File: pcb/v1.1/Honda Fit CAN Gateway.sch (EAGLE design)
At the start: 23 parts, among them U1 TEENSY_3.1_BASIC, U2 MCP2515TSOP, U3 TJA1050, U4 TJA1050, U5 CB3, X1 CON_10X2F_JAE_MX34020NF1

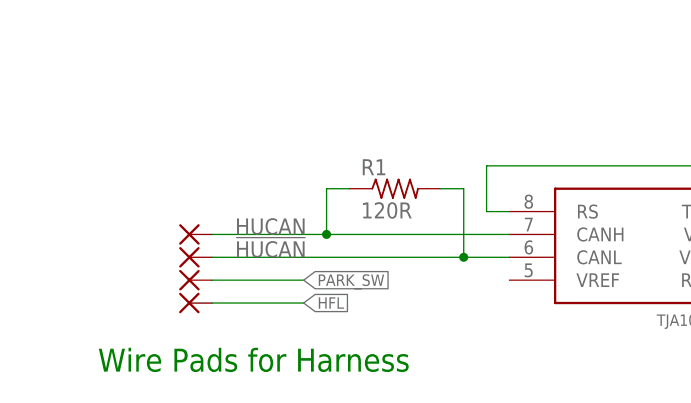
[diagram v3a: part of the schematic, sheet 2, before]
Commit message: Replace discrete pads for output with pin header footprint
Pads were too large on rev 1, and square orientation was not ideal
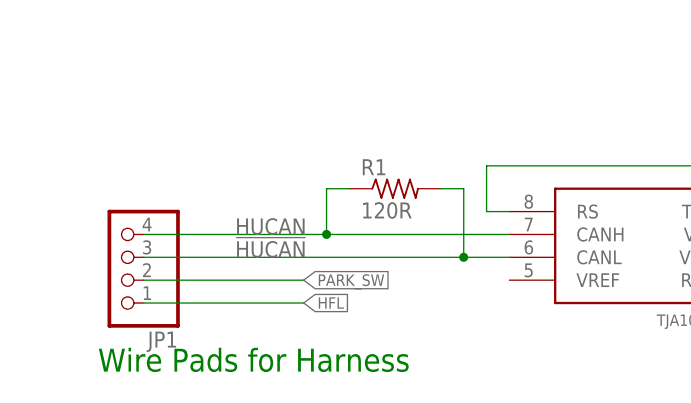
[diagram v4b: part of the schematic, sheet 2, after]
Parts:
- removed PAD1, PAD2, PAD3, PAD4: (no value), wirepad:3,17/1,3
- added JP1: (no value), pinhead:PINHD-1X4
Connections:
- net !HUCAN: now also JP1.3; no longer PAD2.P
- net HFL: now also JP1.1; no longer PAD4.P
- net HUCAN: now also JP1.4; no longer PAD1.P
- net PARK_SW: now also JP1.2; no longer PAD3.P
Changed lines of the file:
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@@
 <part name="SUPPLY2" library="supply2" deviceset="GND" device=""/>
 <part name="P+2" library="supply1" deviceset="+5V" device=""/>
-<part name="PAD1" library="wirepad" deviceset="3,17/1,3" device=""/>
-<part name="PAD2" library="wirepad" deviceset="3,17/1,3" device=""/>
 <part name="FRAME2" library="frames" deviceset="FRAME_A_L" device=""/>
-<part name="PAD3" library="wirepad" deviceset="3,17/1,3" device=""/>
-<part name="PAD4" library="wirepad" deviceset="3,17/1,3" device=""/>
 <part name="FRAME1" library="frames" deviceset="FRAME_A_L" device=""/>
 <part name="P+3" library="supply1" deviceset="+5V" device=""/>
@@
 <part name="C1" library="resistor" deviceset="C-EU" device="C0603" value="100n"/>
 <part name="SUPPLY7" library="supply2" deviceset="GND" device=""/>
+<part name="JP1" library="pinhead" deviceset="PINHD-1X4" device=""/>
 </parts>
 <sheets>
@@
 <attribute name="VALUE" x="208.28" y="147.32" size="1.778" layer="96" rot="R180"/>
 </instance>
-<instance part="PAD1" gate="1" x="88.9" y="71.12" smashed="yes"/>
-<instance part="PAD2" gate="1" x="88.9" y="68.58" smashed="yes"/>
 <instance part="FRAME2" gate="G$1" x="0" y="0"/>
 <instance part="FRAME2" gate="G$2" x="172.72" y="0"/>
-<instance part="PAD3" gate="1" x="88.9" y="66.04" smashed="yes"/>
-<instance part="PAD4" gate="1" x="88.9" y="63.5" smashed="yes"/>
 <instance part="R1" gate="G$1" x="111.76" y="76.2"/>
 <instance part="R4" gate="G$1" x="147.32" y="127"/>
+<instance part="JP1" gate="A" x="81.28" y="68.58" rot="R180"/>
 </instances>
 <busses>
@@
 </segment>
 <segment>
-<pinref part="PAD3" gate="1" pin="P"/>
-<wire x1="91.44" y1="66.04" x2="101.6" y2="66.04" width="0.1524" layer="91"/>
+<wire x1="83.82" y1="66.04" x2="101.6" y2="66.04" width="0.1524" layer="91"/>
 <label x="101.6" y="66.04" size="1.27" layer="95" xref="yes"/>
+<pinref part="JP1" gate="A" pin="2"/>
 </segment>
 </net>
@@
 </segment>
 <segment>
-<pinref part="PAD4" gate="1" pin="P"/>
-<wire x1="91.44" y1="63.5" x2="101.6" y2="63.5" width="0.1524" layer="91"/>
+<wire x1="83.82" y1="63.5" x2="101.6" y2="63.5" width="0.1524" layer="91"/>
 <label x="101.6" y="63.5" size="1.27" layer="95" xref="yes"/>
+<pinref part="JP1" gate="A" pin="1"/>
 </segment>
 </net>
@@
 <wire x1="124.46" y1="71.12" x2="104.14" y2="71.12" width="0.1524" layer="91"/>
 <label x="93.98" y="71.12" size="1.778" layer="95"/>
-<pinref part="PAD1" gate="1" pin="P"/>
 <pinref part="R1" gate="G$1" pin="1"/>
-<wire x1="104.14" y1="71.12" x2="91.44" y2="71.12" width="0.1524" layer="91"/>
+<wire x1="104.14" y1="71.12" x2="83.82" y2="71.12" width="0.1524" layer="91"/>
 <wire x1="106.68" y1="76.2" x2="104.14" y2="76.2" width="0.1524" layer="91"/>
 <wire x1="104.14" y1="76.2" x2="104.14" y2="71.12" width="0.1524" layer="91"/>
 <junction x="104.14" y="71.12"/>
+<pinref part="JP1" gate="A" pin="4"/>
 </segment>
 </net>
@@
 <wire x1="124.46" y1="68.58" x2="119.38" y2="68.58" width="0.1524" layer="91"/>
 <label x="93.98" y="68.58" size="1.778" layer="95"/>
-<pinref part="PAD2" gate="1" pin="P"/>
 <pinref part="R1" gate="G$1" pin="2"/>
-<wire x1="119.38" y1="68.58" x2="91.44" y2="68.58" width="0.1524" layer="91"/>
+<wire x1="119.38" y1="68.58" x2="83.82" y2="68.58" width="0.1524" layer="91"/>
 <wire x1="116.84" y1="76.2" x2="119.38" y2="76.2" width="0.1524" layer="91"/>
 <wire x1="119.38" y1="76.2" x2="119.38" y2="68.58" width="0.1524" layer="91"/>
 <junction x="119.38" y="68.58"/>
-</segment>
-</net>
+<pinref part="JP1" gate="A" pin="3"/>
+</segment>
+</net>

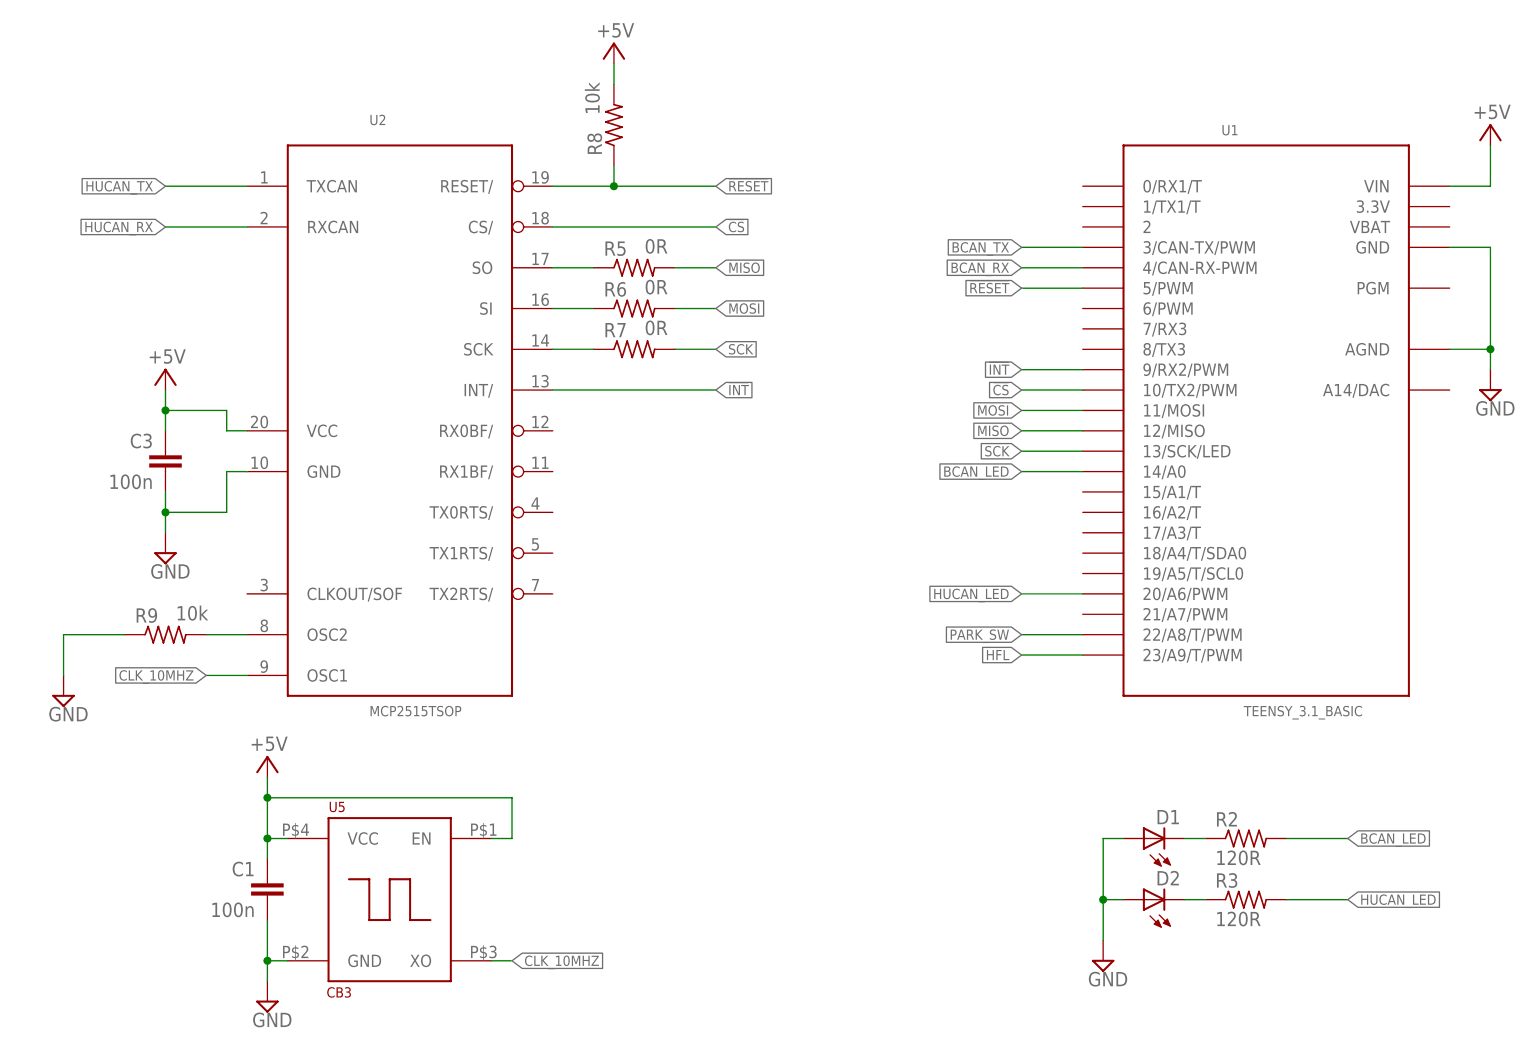
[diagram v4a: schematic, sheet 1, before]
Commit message: Major additions and changes
Added jumper resistors between Park and HFL nets and the Teensy to allow decoupling.  Added land for inductor on MCP2515 +5V rail (805 resistor package).  Reordered some pins to make layout easier.
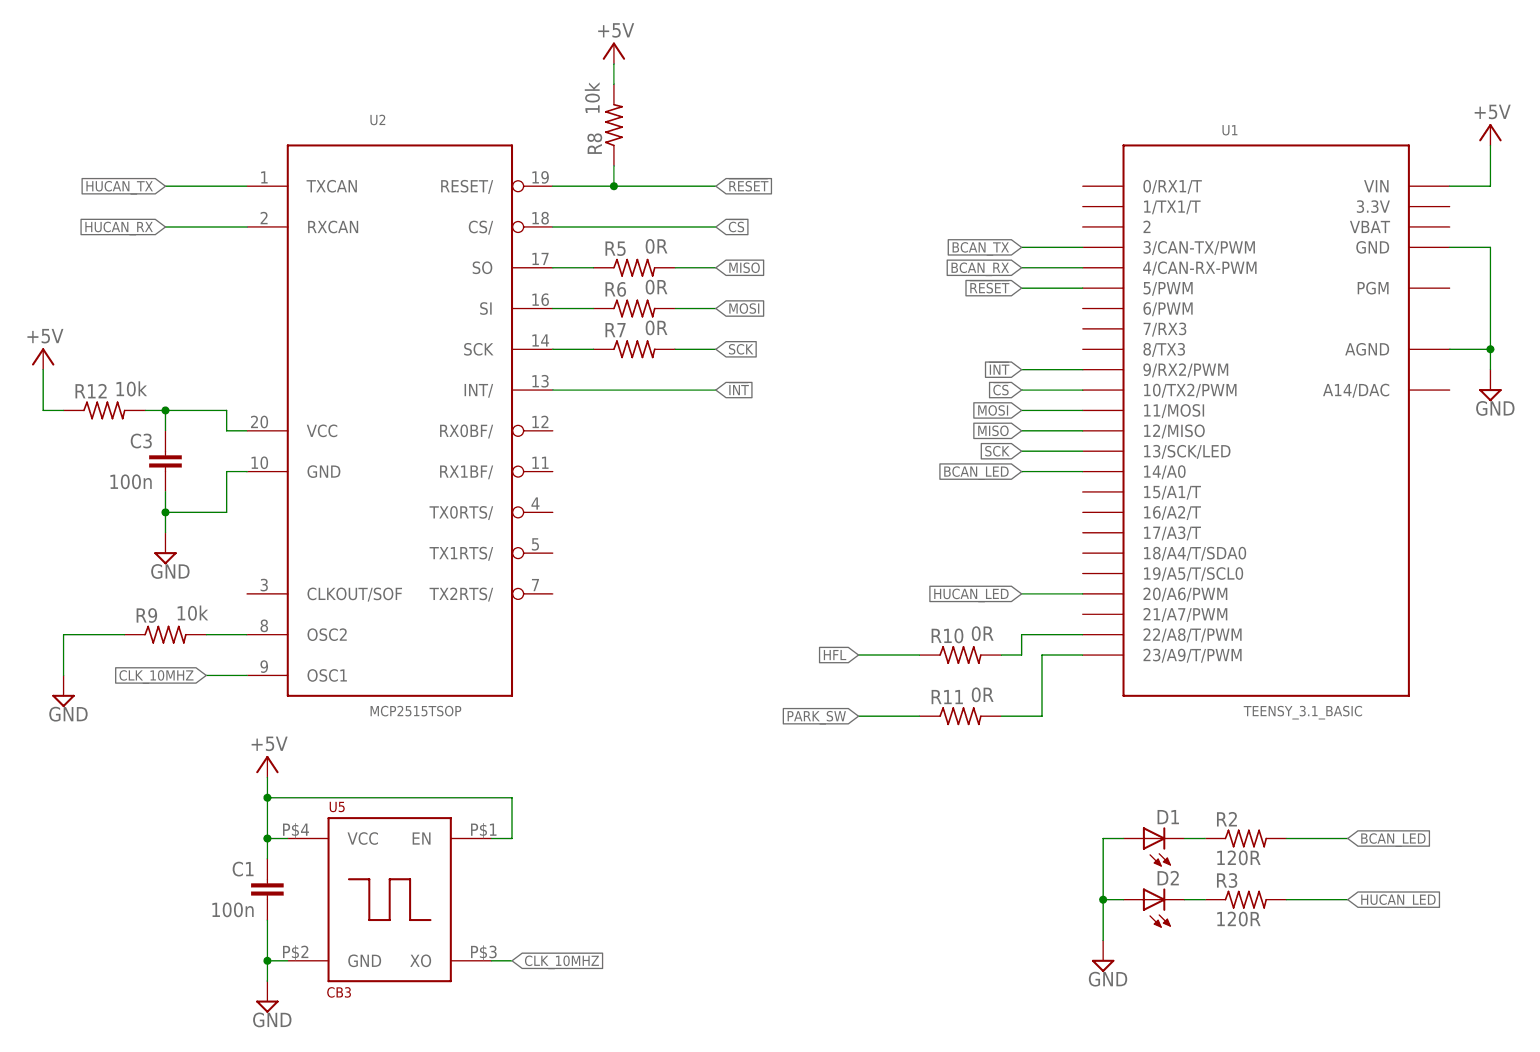
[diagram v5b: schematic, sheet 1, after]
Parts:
- added R10, R11: 0R, resistor:R-US_R0805
- added R12: 10k, resistor:R-US_R0805
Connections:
- new net N$2: R10.2, U1.22/A8/T/PWM
- new net N$3: R11.2, U1.23/A9/T/PWM
- new net N$9: C3.1, R12.2, U2.VCC
- net !HUCAN: now also JP1.4; no longer JP1.3
- net +5V: now also R12.1; no longer C3.1, U2.VCC
- net HFL: now also R10.1; no longer U1.23/A9/T/PWM
- net HUCAN: now also JP1.3; no longer JP1.4
- net PARK_SW: now also R11.1; no longer U1.22/A8/T/PWM
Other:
- moved on the sheet: JP1
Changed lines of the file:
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@@
 <part name="SUPPLY1" library="supply2" deviceset="GND" device=""/>
 <part name="U2" library="MCP2515_MT" deviceset="MCP2515*" device="TSOP"/>
-<part name="P+4" library="supply1" deviceset="+5V" device=""/>
 <part name="SUPPLY4" library="supply2" deviceset="GND" device=""/>
 <part name="SUPPLY5" library="supply2" deviceset="GND" device=""/>
@@
 <part name="SUPPLY7" library="supply2" deviceset="GND" device=""/>
 <part name="JP1" library="pinhead" deviceset="PINHD-1X4" device=""/>
+<part name="R10" library="resistor" deviceset="R-US_" device="R0805" value="0R"/>
+<part name="R11" library="resistor" deviceset="R-US_" device="R0805" value="0R"/>
+<part name="R12" library="resistor" deviceset="R-US_" device="R0805" value="10k"/>
+<part name="P+7" library="supply1" deviceset="+5V" device=""/>
 </parts>
 <sheets>
@@
 <instance part="SUPPLY1" gate="GND" x="218.44" y="147.32"/>
 <instance part="U2" gate="G$1" x="81.28" y="144.78"/>
-<instance part="P+4" gate="1" x="53.34" y="149.86" smashed="yes">
-<attribute name="VALUE" x="55.88" y="152.4" size="1.778" layer="96" rot="R180"/>
-</instance>
 <instance part="SUPPLY4" gate="GND" x="53.34" y="127"/>
 <instance part="SUPPLY5" gate="GND" x="40.64" y="109.22"/>
@@
 <instance part="C1" gate="G$1" x="66.04" y="86.36" rot="MR0"/>
 <instance part="SUPPLY7" gate="GND" x="66.04" y="71.12"/>
+<instance part="R10" gate="G$1" x="152.4" y="114.3" smashed="yes">
+<attribute name="NAME" x="148.59" y="115.7986" size="1.778" layer="95"/>
+<attribute name="VALUE" x="153.67" y="116.078" size="1.778" layer="96"/>
+</instance>
+<instance part="R11" gate="G$1" x="152.4" y="106.68" smashed="yes">
+<attribute name="NAME" x="148.59" y="108.1786" size="1.778" layer="95"/>
+<attribute name="VALUE" x="153.67" y="108.458" size="1.778" layer="96"/>
+</instance>
+<instance part="R12" gate="G$1" x="45.72" y="144.78" smashed="yes">
+<attribute name="NAME" x="41.91" y="146.2786" size="1.778" layer="95"/>
+<attribute name="VALUE" x="46.99" y="146.558" size="1.778" layer="96"/>
+</instance>
+<instance part="P+7" gate="1" x="38.1" y="152.4" smashed="yes">
+<attribute name="VALUE" x="40.64" y="154.94" size="1.778" layer="96" rot="R180"/>
+</instance>
 </instances>
 <busses>
@@
 <wire x1="213.36" y1="172.72" x2="218.44" y2="172.72" width="0.1524" layer="91"/>
 <wire x1="218.44" y1="172.72" x2="218.44" y2="177.8" width="0.1524" layer="91"/>
-</segment>
-<segment>
-<pinref part="P+4" gate="1" pin="+5V"/>
-<wire x1="53.34" y1="147.32" x2="53.34" y2="144.78" width="0.1524" layer="91"/>
-<wire x1="53.34" y1="144.78" x2="60.96" y2="144.78" width="0.1524" layer="91"/>
-<wire x1="60.96" y1="144.78" x2="60.96" y2="142.24" width="0.1524" layer="91"/>
-<pinref part="U2" gate="G$1" pin="VCC"/>
-<wire x1="60.96" y1="142.24" x2="63.5" y2="142.24" width="0.1524" layer="91"/>
-<pinref part="C3" gate="G$1" pin="1"/>
-<wire x1="53.34" y1="144.78" x2="53.34" y2="142.24" width="0.1524" layer="91"/>
-<junction x="53.34" y="144.78"/>
 </segment>
 <segment>
@@
 <junction x="66.04" y="91.44"/>
 </segment>
+<segment>
+<pinref part="P+7" gate="1" pin="+5V"/>
+<wire x1="38.1" y1="149.86" x2="38.1" y2="144.78" width="0.1524" layer="91"/>
+<pinref part="R12" gate="G$1" pin="1"/>
+<wire x1="38.1" y1="144.78" x2="40.64" y2="144.78" width="0.1524" layer="91"/>
+</segment>
 </net>
 <net name="HUCAN_RX" class="0">
@@
 <wire x1="63.5" y1="172.72" x2="53.34" y2="172.72" width="0.1524" layer="91"/>
 <label x="53.34" y="172.72" size="1.27" layer="95" rot="R180" xref="yes"/>
-</segment>
-</net>
-<net name="PARK_SW" class="0">
-<segment>
-<pinref part="U1" gate="G$1" pin="22/A8/T/PWM"/>
-<wire x1="167.64" y1="116.84" x2="160.02" y2="116.84" width="0.1524" layer="91"/>
-<label x="160.02" y="116.84" size="1.27" layer="95" rot="R180" xref="yes"/>
-</segment>
-</net>
-<net name="HFL" class="0">
-<segment>
-<pinref part="U1" gate="G$1" pin="23/A9/T/PWM"/>
-<wire x1="167.64" y1="114.3" x2="160.02" y2="114.3" width="0.1524" layer="91"/>
-<label x="160.02" y="114.3" size="1.27" layer="95" rot="R180" xref="yes"/>
 </segment>
 </net>
@@
 <wire x1="93.98" y1="76.2" x2="96.52" y2="76.2" width="0.1524" layer="91"/>
 <label x="96.52" y="76.2" size="1.27" layer="95" xref="yes"/>
+</segment>
+</net>
+<net name="HFL" class="0">
+<segment>
+<label x="139.7" y="114.3" size="1.27" layer="95" rot="R180" xref="yes"/>
+<pinref part="R10" gate="G$1" pin="1"/>
+<wire x1="139.7" y1="114.3" x2="147.32" y2="114.3" width="0.1524" layer="91"/>
+</segment>
+</net>
+<net name="PARK_SW" class="0">
+<segment>
+<label x="139.7" y="106.68" size="1.27" layer="95" rot="R180" xref="yes"/>
+<pinref part="R11" gate="G$1" pin="1"/>
+<wire x1="139.7" y1="106.68" x2="147.32" y2="106.68" width="0.1524" layer="91"/>
+</segment>
+</net>
+<net name="N$2" class="0">
+<segment>
+<pinref part="R10" gate="G$1" pin="2"/>
+<wire x1="157.48" y1="114.3" x2="160.02" y2="114.3" width="0.1524" layer="91"/>
+<wire x1="160.02" y1="114.3" x2="160.02" y2="116.84" width="0.1524" layer="91"/>
+<pinref part="U1" gate="G$1" pin="22/A8/T/PWM"/>
+<wire x1="160.02" y1="116.84" x2="167.64" y2="116.84" width="0.1524" layer="91"/>
+</segment>
+</net>
+<net name="N$3" class="0">
+<segment>
+<pinref part="R11" gate="G$1" pin="2"/>
+<wire x1="157.48" y1="106.68" x2="162.56" y2="106.68" width="0.1524" layer="91"/>
+<wire x1="162.56" y1="106.68" x2="162.56" y2="114.3" width="0.1524" layer="91"/>
+<pinref part="U1" gate="G$1" pin="23/A9/T/PWM"/>
+<wire x1="162.56" y1="114.3" x2="167.64" y2="114.3" width="0.1524" layer="91"/>
+</segment>
+</net>
+<net name="N$9" class="0">
+<segment>
+<wire x1="53.34" y1="144.78" x2="60.96" y2="144.78" width="0.1524" layer="91"/>
+<wire x1="60.96" y1="144.78" x2="60.96" y2="142.24" width="0.1524" layer="91"/>
+<pinref part="U2" gate="G$1" pin="VCC"/>
+<wire x1="60.96" y1="142.24" x2="63.5" y2="142.24" width="0.1524" layer="91"/>
+<pinref part="C3" gate="G$1" pin="1"/>
+<wire x1="53.34" y1="144.78" x2="53.34" y2="142.24" width="0.1524" layer="91"/>
+<pinref part="R12" gate="G$1" pin="2"/>
+<wire x1="50.8" y1="144.78" x2="53.34" y2="144.78" width="0.1524" layer="91"/>
+<junction x="53.34" y="144.78"/>
 </segment>
 </net>
@@
 <instance part="R1" gate="G$1" x="111.76" y="76.2"/>
 <instance part="R4" gate="G$1" x="147.32" y="127"/>
-<instance part="JP1" gate="A" x="81.28" y="68.58" rot="R180"/>
+<instance part="JP1" gate="A" x="71.12" y="71.12" rot="MR0"/>
 </instances>
 <busses>
@@
 </segment>
 <segment>
-<wire x1="83.82" y1="66.04" x2="101.6" y2="66.04" width="0.1524" layer="91"/>
-<label x="101.6" y="66.04" size="1.27" layer="95" xref="yes"/>
+<wire x1="73.66" y1="73.66" x2="81.28" y2="73.66" width="0.1524" layer="91"/>
+<wire x1="81.28" y1="73.66" x2="81.28" y2="78.74" width="0.1524" layer="91"/>
+<wire x1="81.28" y1="78.74" x2="83.82" y2="78.74" width="0.1524" layer="91"/>
+<label x="83.82" y="78.74" size="1.27" layer="95" xref="yes"/>
 <pinref part="JP1" gate="A" pin="2"/>
 </segment>
@@
 </segment>
 <segment>
-<wire x1="83.82" y1="63.5" x2="101.6" y2="63.5" width="0.1524" layer="91"/>
-<label x="101.6" y="63.5" size="1.27" layer="95" xref="yes"/>
+<wire x1="73.66" y1="76.2" x2="78.74" y2="76.2" width="0.1524" layer="91"/>
+<wire x1="78.74" y1="76.2" x2="78.74" y2="81.28" width="0.1524" layer="91"/>
+<wire x1="78.74" y1="81.28" x2="83.82" y2="81.28" width="0.1524" layer="91"/>
+<label x="83.82" y="81.28" size="1.27" layer="95" xref="yes"/>
 <pinref part="JP1" gate="A" pin="1"/>
 </segment>
@@
 <label x="93.98" y="71.12" size="1.778" layer="95"/>
 <pinref part="R1" gate="G$1" pin="1"/>
-<wire x1="104.14" y1="71.12" x2="83.82" y2="71.12" width="0.1524" layer="91"/>
 <wire x1="106.68" y1="76.2" x2="104.14" y2="76.2" width="0.1524" layer="91"/>
 <wire x1="104.14" y1="76.2" x2="104.14" y2="71.12" width="0.1524" layer="91"/>
+<pinref part="JP1" gate="A" pin="3"/>
+<wire x1="104.14" y1="71.12" x2="73.66" y2="71.12" width="0.1524" layer="91"/>
 <junction x="104.14" y="71.12"/>
-<pinref part="JP1" gate="A" pin="4"/>
 </segment>
 </net>
@@
 <label x="93.98" y="68.58" size="1.778" layer="95"/>
 <pinref part="R1" gate="G$1" pin="2"/>
-<wire x1="119.38" y1="68.58" x2="83.82" y2="68.58" width="0.1524" layer="91"/>
 <wire x1="116.84" y1="76.2" x2="119.38" y2="76.2" width="0.1524" layer="91"/>
 <wire x1="119.38" y1="76.2" x2="119.38" y2="68.58" width="0.1524" layer="91"/>
+<pinref part="JP1" gate="A" pin="4"/>
+<wire x1="73.66" y1="68.58" x2="119.38" y2="68.58" width="0.1524" layer="91"/>
 <junction x="119.38" y="68.58"/>
-<pinref part="JP1" gate="A" pin="3"/>
-</segment>
-</net>
+</segment>
+</net>

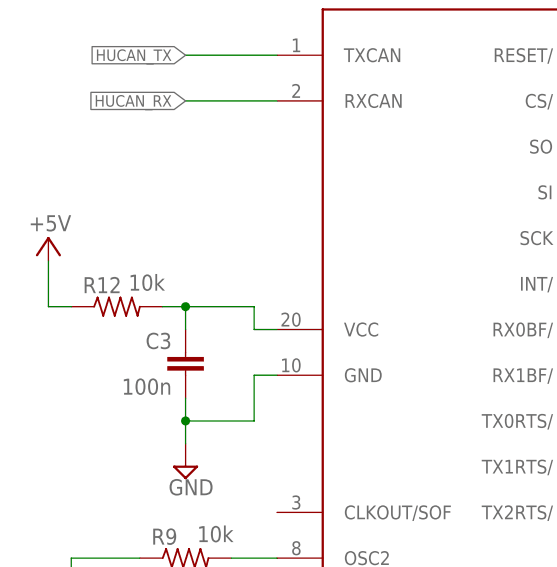
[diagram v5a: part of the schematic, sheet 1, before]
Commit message: Change resistor value
Change resistor land used for MCP2515 supply inductor to be 0 ohms for clarity
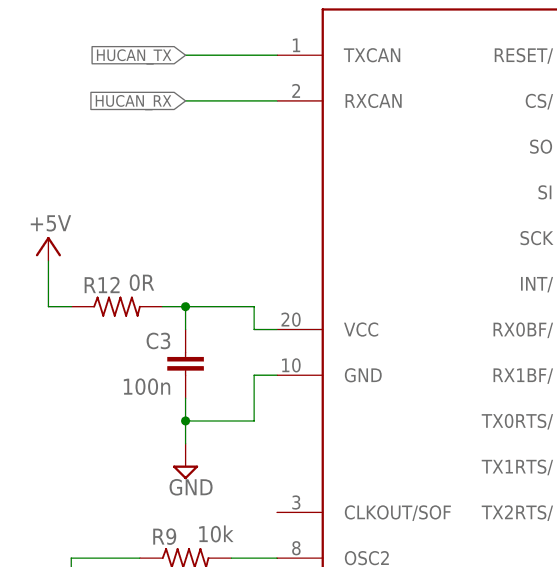
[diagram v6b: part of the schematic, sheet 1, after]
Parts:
- R12: value 10k -> 0R
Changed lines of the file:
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@@
 <part name="R10" library="resistor" deviceset="R-US_" device="R0805" value="0R"/>
 <part name="R11" library="resistor" deviceset="R-US_" device="R0805" value="0R"/>
-<part name="R12" library="resistor" deviceset="R-US_" device="R0805" value="10k"/>
+<part name="R12" library="resistor" deviceset="R-US_" device="R0805" value="0R"/>
 <part name="P+7" library="supply1" deviceset="+5V" device=""/>
 </parts>
